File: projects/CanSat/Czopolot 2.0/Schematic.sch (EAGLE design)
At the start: 117 parts

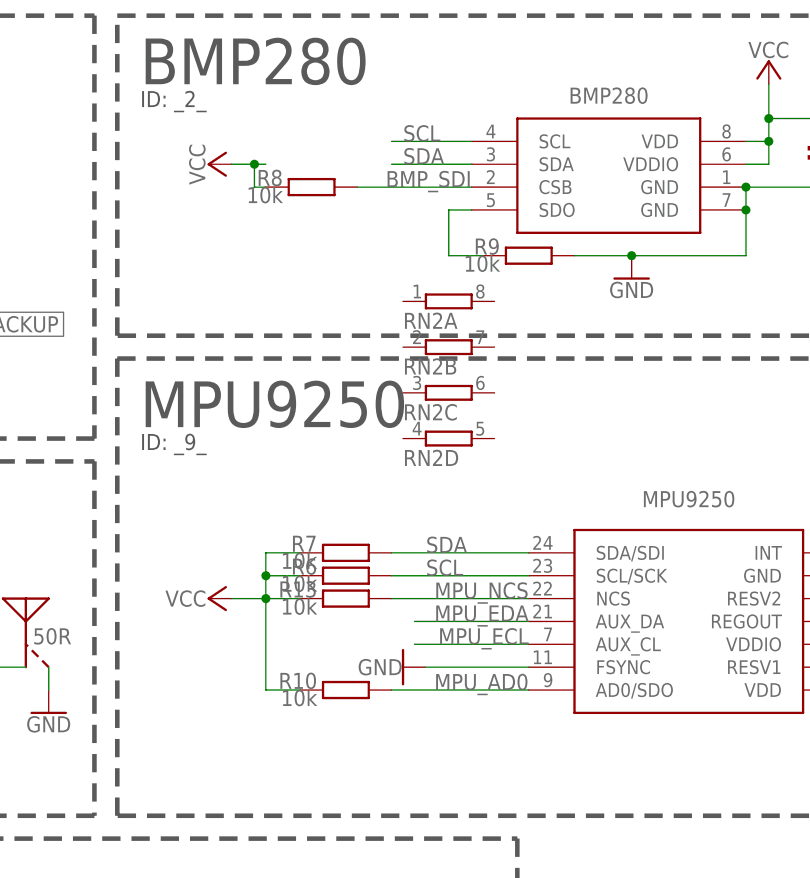
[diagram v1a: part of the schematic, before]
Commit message: Screwholes added
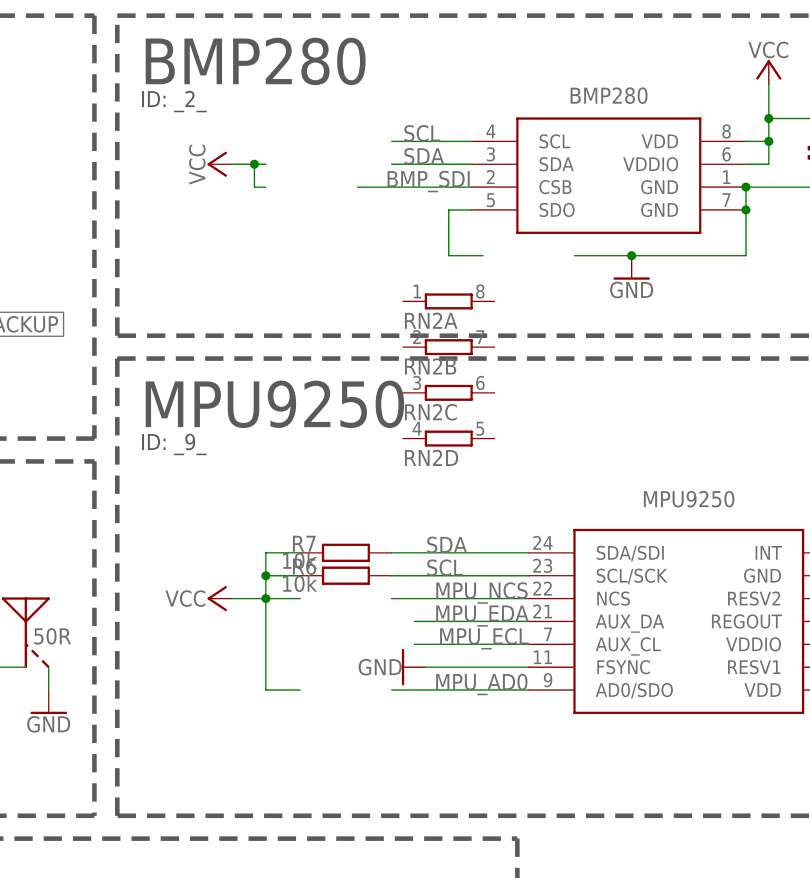
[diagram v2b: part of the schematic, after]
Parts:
- removed R10, R13, R8, R9: 10k, Unified:RESISTOR0603
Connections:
- net BMP_SDI: no longer R8.1
- net BMP_SDO: no longer R9.2
- net GND: no longer R9.1
- net MPU_AD0: no longer R10.1
- net MPU_NCS: no longer R13.1
- net VCC: no longer R10.2, R13.2, R8.2
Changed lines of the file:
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@@
 <part name="GND31" library="supply1" library_urn="urn:adsk.eagle:library:371" deviceset="GND" device=""/>
 <part name="GND32" library="supply1" library_urn="urn:adsk.eagle:library:371" deviceset="GND" device=""/>
-<part name="R8" library="Unified" deviceset="RESISTOR" device="0603" package3d_urn="urn:adsk.eagle:package:23555/3" value="10k"/>
-<part name="R9" library="Unified" deviceset="RESISTOR" device="0603" package3d_urn="urn:adsk.eagle:package:23555/3" value="10k"/>
-<part name="R10" library="Unified" deviceset="RESISTOR" device="0603" package3d_urn="urn:adsk.eagle:package:23555/3" value="10k"/>
-<part name="R13" library="Unified" deviceset="RESISTOR" device="0603" package3d_urn="urn:adsk.eagle:package:23555/3" value="10k"/>
 <part name="U$5" library="SobieskiSat2" deviceset="OSCILLATOR_2PIN" device="32X15" package3d_urn="urn:adsk.eagle:package:16206908/2" value="32.768kHz"/>
 <part name="U$6" library="SobieskiSat2" deviceset="OSCILLATOR_4PIN" device="32X25" package3d_urn="urn:adsk.eagle:package:15725817/1" value="12MHz"/>
@@
 <attribute name="VALUE" x="233.68" y="26.67" size="1.778" layer="96" align="center"/>
 </instance>
-<instance part="R8" gate="R$1" x="226.06" y="80.01" smashed="yes" rot="R90">
-<attribute name="NAME" x="222.885" y="81.915" size="1.778" layer="95" rot="R180"/>
-<attribute name="VALUE" x="222.885" y="80.01" size="1.778" layer="96" rot="R180"/>
-</instance>
-<instance part="R9" gate="R$1" x="250.19" y="72.39" smashed="yes" rot="R90">
-<attribute name="NAME" x="247.015" y="74.295" size="1.778" layer="95" rot="R180"/>
-<attribute name="VALUE" x="247.015" y="72.39" size="1.778" layer="96" rot="R180"/>
-</instance>
-<instance part="R10" gate="R$1" x="229.87" y="24.13" smashed="yes" rot="R90">
-<attribute name="NAME" x="226.695" y="26.035" size="1.778" layer="95" rot="R180"/>
-<attribute name="VALUE" x="226.695" y="24.13" size="1.778" layer="96" rot="R180"/>
-</instance>
-<instance part="R13" gate="R$1" x="229.87" y="34.29" smashed="yes" rot="R90">
-<attribute name="NAME" x="226.695" y="36.195" size="1.778" layer="95" rot="R180"/>
-<attribute name="VALUE" x="226.695" y="34.29" size="1.778" layer="96" rot="R180"/>
-</instance>
 <instance part="U$5" gate="G$1" x="68.58" y="50.8" smashed="yes">
 <attribute name="VALUE" x="68.58" y="55.88" size="1.27" layer="96" align="center"/>
@@
 <pinref part="P+13" gate="VCC" pin="VCC"/>
 <wire x1="217.17" y1="34.29" x2="220.98" y2="34.29" width="0.1524" layer="91"/>
-<pinref part="R10" gate="R$1" pin="2"/>
 <wire x1="220.98" y1="24.13" x2="224.79" y2="24.13" width="0.1524" layer="91"/>
 <wire x1="224.79" y1="34.29" x2="220.98" y2="34.29" width="0.1524" layer="91"/>
-<pinref part="R13" gate="R$1" pin="2"/>
 <pinref part="R7" gate="R$1" pin="2"/>
 <wire x1="224.79" y1="39.37" x2="220.98" y2="39.37" width="0.1524" layer="91"/>
@@
 <wire x1="220.98" y1="82.55" x2="219.71" y2="82.55" width="0.1524" layer="91"/>
 <junction x="219.71" y="82.55"/>
-<pinref part="R8" gate="R$1" pin="2"/>
 <wire x1="219.71" y1="82.55" x2="219.71" y2="80.01" width="0.1524" layer="91"/>
 <wire x1="219.71" y1="80.01" x2="220.98" y2="80.01" width="0.1524" layer="91"/>
@@
 </segment>
 <segment>
-<pinref part="R9" gate="R$1" pin="1"/>
 <pinref part="U$8" gate="G$1" pin="GND@2"/>
 <wire x1="255.27" y1="72.39" x2="261.62" y2="72.39" width="0.1524" layer="91"/>
@@
 <wire x1="243.84" y1="80.01" x2="231.14" y2="80.01" width="0.1524" layer="91"/>
 <label x="243.84" y="80.01" size="1.778" layer="95" align="bottom-right"/>
-<pinref part="R8" gate="R$1" pin="1"/>
 </segment>
 </net>
@@
 <wire x1="241.3" y1="77.47" x2="241.3" y2="72.39" width="0.1524" layer="91"/>
 <wire x1="241.3" y1="72.39" x2="245.11" y2="72.39" width="0.1524" layer="91"/>
-<pinref part="R9" gate="R$1" pin="2"/>
 </segment>
 </net>
@@
 <wire x1="250.19" y1="34.29" x2="234.95" y2="34.29" width="0.1524" layer="91"/>
 <label x="250.19" y="34.29" size="1.778" layer="95" align="bottom-right"/>
-<pinref part="R13" gate="R$1" pin="1"/>
 </segment>
 </net>
@@
 <wire x1="234.95" y1="24.13" x2="250.19" y2="24.13" width="0.1524" layer="91"/>
 <label x="250.19" y="24.13" size="1.778" layer="95" align="bottom-right"/>
-<pinref part="R10" gate="R$1" pin="1"/>
-</segment>
-</net>
+</segment>
+</net>

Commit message: Version 0.5
Pre-final component placement
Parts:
- removed C38, C39: big_pol, Unified:CAPACITOR0603
- removed C5: 4.7u, Unified:CAPACITOR0603
- added U$33, U$34: PADOCT, Unified:PADOCT
- BAT_PACK: device SobieskiSat2:BATTERYDIP -> SobieskiSat2:BATTERYBIG
- BTN_DFU: value PUSH-SWITCH -> PUSH-SWITCHDIP; device SobieskiSat2:PUSH-SWITCH -> SobieskiSat2:PUSH-SWITCHDIP
- U$19, U$29, U$31, U$32: value PAD -> PADRND; device Unified:PAD -> Unified:PADRND
- U$20, U$30: value PAD -> PADOCT; device Unified:PAD -> Unified:PADOCT
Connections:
- net GND: now also U$33.1, U$34.1; no longer C38.1, C39.1, C5.2, U$32.1
- net VCC: now also U$32.1; no longer C5.1
- net VSYS: no longer C38.2, C39.2
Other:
- note added: "4.7u was there"

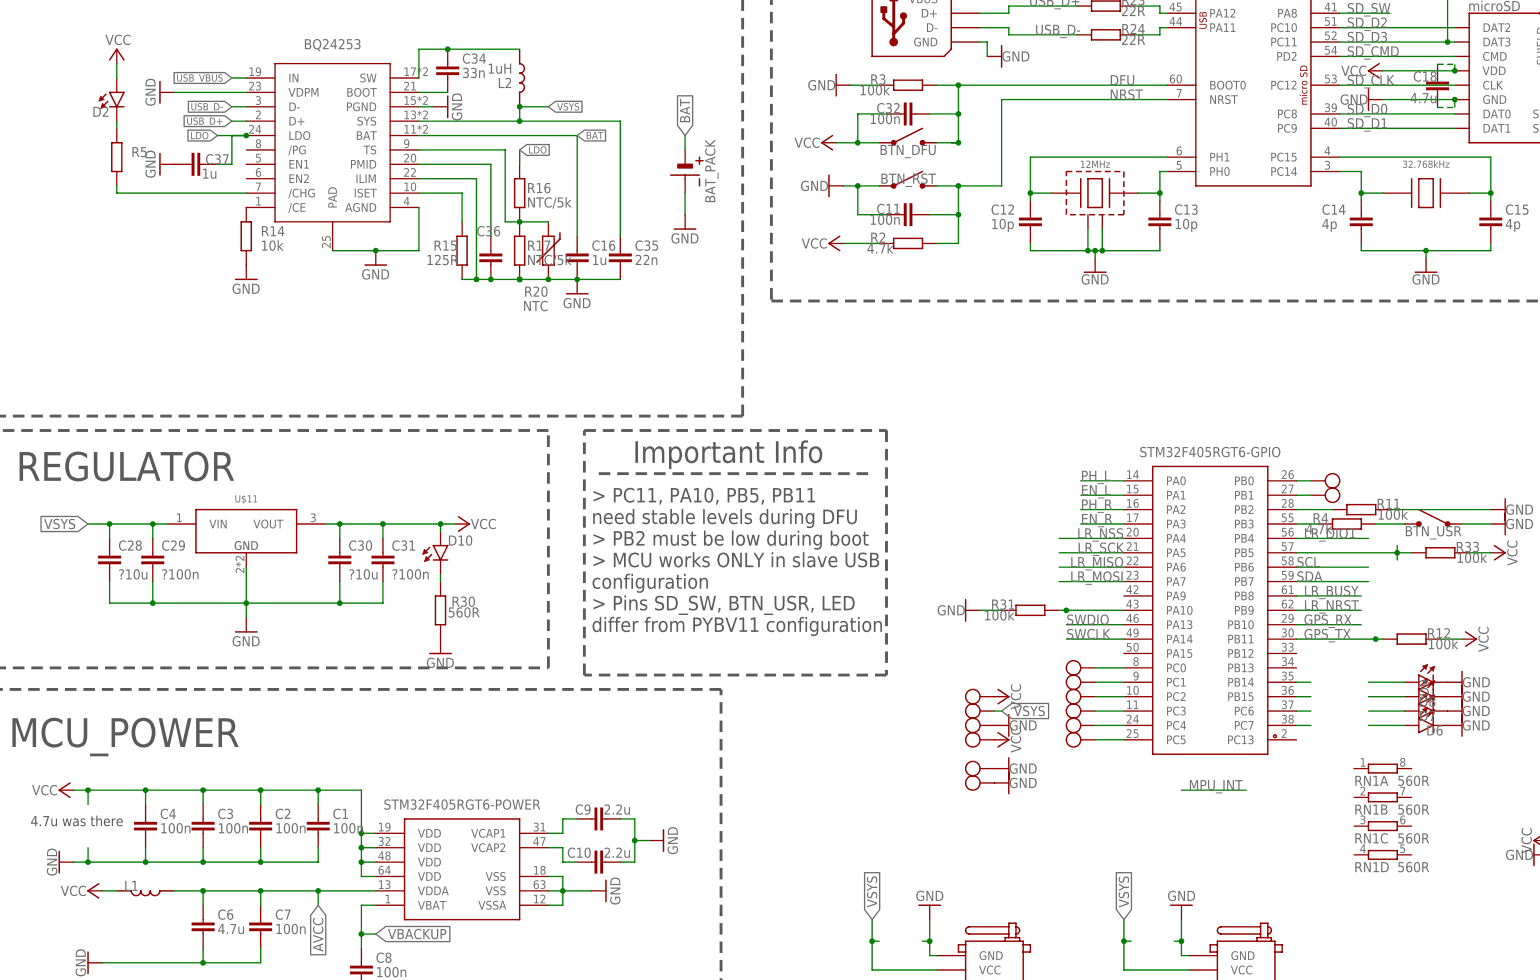
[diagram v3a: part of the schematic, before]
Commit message: Round traces test
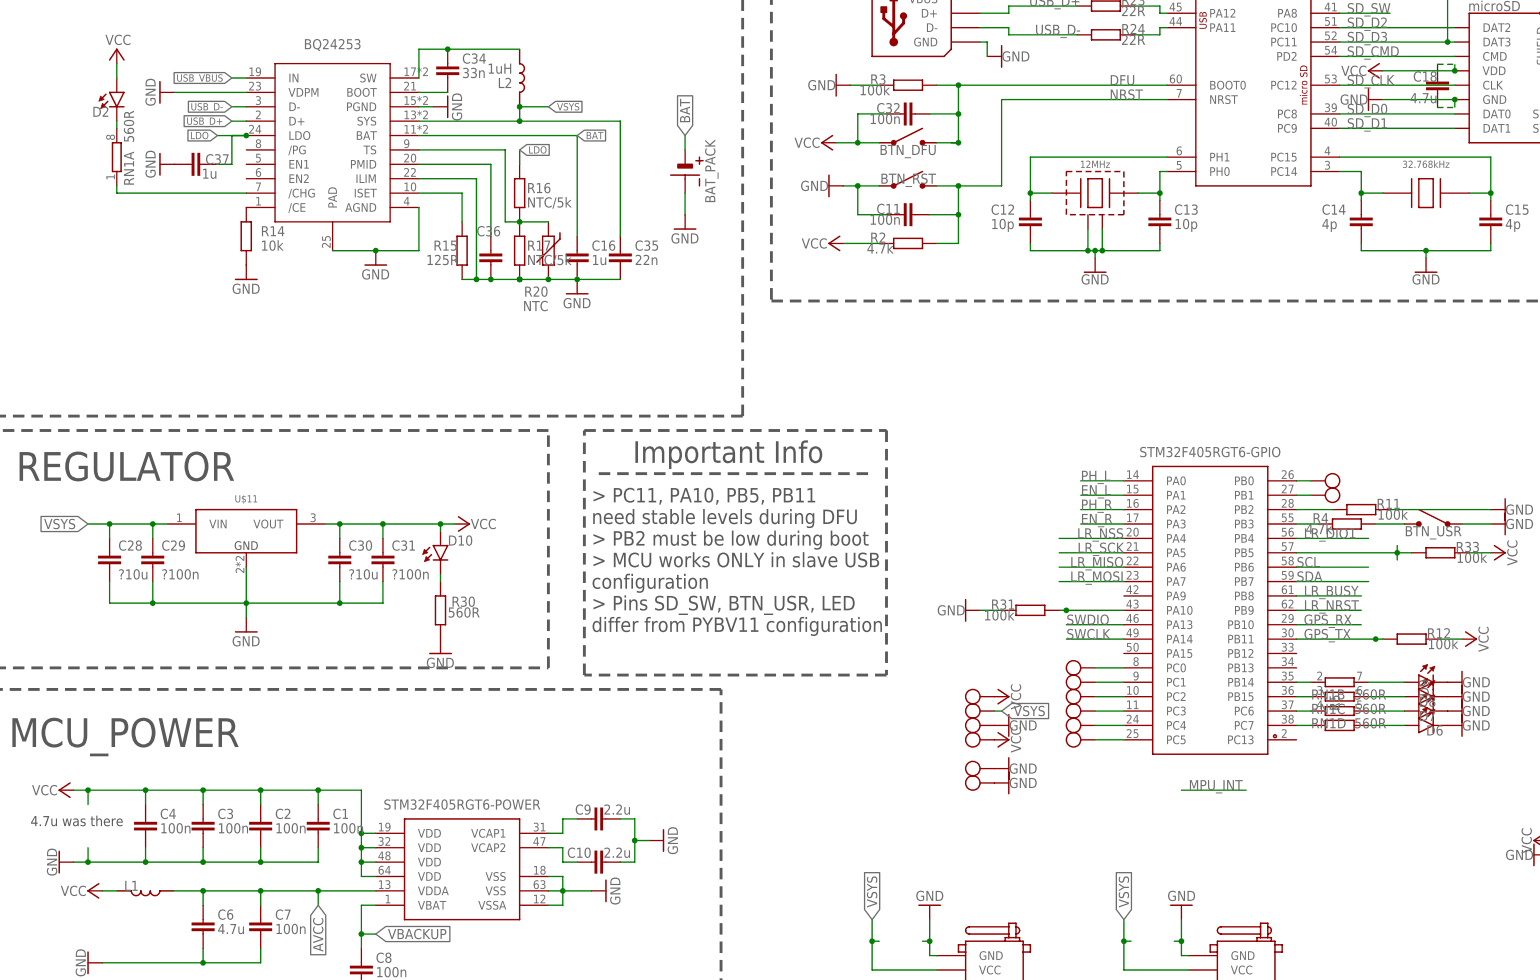
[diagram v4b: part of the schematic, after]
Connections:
- net N$1: now also RN1B.2
- net N$10: now also RN1A.1; no longer R5.1
- net N$15: now also R5.2
- net N$19: now also RN1D.1
- net N$2: now also RN1C.2
- net N$20: now also RN1C.1
- net N$28: now also RN1B.1
- net N$3: now also RN1A.2; no longer R5.2
- net N$37: now also RN1D.2
- net N$38: now also R5.1
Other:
- moved on the sheet: R5, RN1A, RN1B, RN1C, RN1D
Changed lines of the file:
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@@
 <setting verticaltext="up"/>
 </settings>
-<grid distance="0.1" unitdist="inch" unit="inch" style="lines" multiple="1" display="no" altdistance="0.01" altunitdist="inch" altunit="inch"/>
+<grid distance="0.05" unitdist="inch" unit="inch" style="lines" multiple="1" display="no" altdistance="0.01" altunitdist="inch" altunit="inch"/>
 <layers>
 <layer number="1" name="Top" color="4" fill="1" visible="no" active="no"/>
@@
 <part name="GND19" library="supply1" library_urn="urn:adsk.eagle:library:371" deviceset="GND" device=""/>
 <part name="U$10" library="SobieskiSat2" deviceset="BQ24253" device="" package3d_urn="urn:adsk.eagle:package:15841520/1"/>
-<part name="R5" library="Unified" deviceset="RESISTOR" device="0603" package3d_urn="urn:adsk.eagle:package:23555/3"/>
 <part name="R14" library="Unified" deviceset="RESISTOR" device="0603" package3d_urn="urn:adsk.eagle:package:23555/3" value="10k"/>
 <part name="R15" library="Unified" deviceset="RESISTOR" device="0603" package3d_urn="urn:adsk.eagle:package:23555/3" value="125R"/>
@@
 <part name="U$34" library="Unified" deviceset="PAD" device="OCT" value="PADOCT"/>
 <part name="GND45" library="supply1" library_urn="urn:adsk.eagle:library:371" deviceset="GND" device=""/>
+<part name="R5" library="Unified" deviceset="RESISTOR" device="0603" package3d_urn="urn:adsk.eagle:package:23555/3"/>
 </parts>
 <sheets>
@@
 </instance>
 <instance part="U$10" gate="G$1" x="-124.46" y="58.42" smashed="yes"/>
-<instance part="R5" gate="R$1" x="-162.56" y="57.15" smashed="yes">
-<attribute name="NAME" x="-160.02" y="57.15" size="1.778" layer="95"/>
-<attribute name="VALUE" x="-160.02" y="54.61" size="1.778" layer="96"/>
-</instance>
 <instance part="R14" gate="R$1" x="-139.7" y="43.18" smashed="yes">
 <attribute name="NAME" x="-137.16" y="43.18" size="1.778" layer="95"/>
@@
 <attribute name="VALUE" x="-86.36" y="31.75" size="1.778" layer="96" rot="R180"/>
 </instance>
-<instance part="RN1" gate="A" x="60.96" y="-50.8" smashed="yes">
-<attribute name="VALUE" x="63.5" y="-53.848" size="1.778" layer="96"/>
-<attribute name="NAME" x="55.88" y="-53.848" size="1.778" layer="95"/>
-</instance>
-<instance part="RN1" gate="B" x="60.96" y="-55.88" smashed="yes">
-<attribute name="VALUE" x="63.5" y="-58.928" size="1.778" layer="96"/>
-<attribute name="NAME" x="55.88" y="-58.928" size="1.778" layer="95"/>
-</instance>
-<instance part="RN1" gate="C" x="60.96" y="-60.96" smashed="yes">
-<attribute name="VALUE" x="63.5" y="-64.008" size="1.778" layer="96"/>
-<attribute name="NAME" x="55.88" y="-64.008" size="1.778" layer="95"/>
-</instance>
-<instance part="RN1" gate="D" x="60.96" y="-66.04" smashed="yes">
-<attribute name="VALUE" x="63.5" y="-69.088" size="1.778" layer="96"/>
-<attribute name="NAME" x="55.88" y="-69.088" size="1.778" layer="95"/>
+<instance part="RN1" gate="A" x="-162.56" y="57.15" smashed="yes" rot="R90">
+<attribute name="VALUE" x="-159.512" y="59.69" size="1.778" layer="96" rot="R90"/>
+<attribute name="NAME" x="-159.512" y="52.07" size="1.778" layer="95" rot="R90"/>
+</instance>
+<instance part="RN1" gate="B" x="53.34" y="-35.56" smashed="yes">
+<attribute name="VALUE" x="55.88" y="-38.608" size="1.778" layer="96"/>
+<attribute name="NAME" x="48.26" y="-38.608" size="1.778" layer="95"/>
+</instance>
+<instance part="RN1" gate="C" x="53.34" y="-38.1" smashed="yes">
+<attribute name="VALUE" x="55.88" y="-41.148" size="1.778" layer="96"/>
+<attribute name="NAME" x="48.26" y="-41.148" size="1.778" layer="95"/>
+</instance>
+<instance part="RN1" gate="D" x="53.34" y="-40.64" smashed="yes">
+<attribute name="VALUE" x="55.88" y="-43.688" size="1.778" layer="96"/>
+<attribute name="NAME" x="48.26" y="-43.688" size="1.778" layer="95"/>
 </instance>
 <instance part="RN2" gate="A" x="241.3" y="67.31" smashed="yes">
@@
 <instance part="GND45" gate="1" x="-5.08" y="-53.34" smashed="yes" rot="MR270">
 <attribute name="VALUE" x="-2.54" y="-53.34" size="1.778" layer="96" rot="MR180" align="center"/>
+</instance>
+<instance part="R5" gate="R$1" x="53.34" y="-43.18" smashed="yes" rot="R90">
+<attribute name="NAME" x="53.34" y="-40.64" size="1.778" layer="95" rot="R90"/>
+<attribute name="VALUE" x="55.88" y="-40.64" size="1.778" layer="96" rot="R90"/>
 </instance>
 </instances>
@@
 <pinref part="D9" gate="G$1" pin="P$1"/>
 <wire x1="58.42" y1="-35.56" x2="64.77" y2="-35.56" width="0.1524" layer="91"/>
+<pinref part="RN1" gate="B" pin="2"/>
 </segment>
 </net>
@@
 <pinref part="D8" gate="G$1" pin="P$1"/>
 <wire x1="58.42" y1="-38.1" x2="64.77" y2="-38.1" width="0.1524" layer="91"/>
+<pinref part="RN1" gate="C" pin="2"/>
 </segment>
 </net>
@@
 <pinref part="D7" gate="G$1" pin="P$1"/>
 <wire x1="58.42" y1="-40.64" x2="64.77" y2="-40.64" width="0.1524" layer="91"/>
+<pinref part="RN1" gate="D" pin="2"/>
 </segment>
 </net>
@@
 <pinref part="D6" gate="G$1" pin="P$1"/>
 <wire x1="58.42" y1="-43.18" x2="64.77" y2="-43.18" width="0.1524" layer="91"/>
+<pinref part="R5" gate="R$1" pin="1"/>
 </segment>
 </net>
@@
 <segment>
 <pinref part="D2" gate="G$1" pin="P$2"/>
-<pinref part="R5" gate="R$1" pin="2"/>
 <wire x1="-162.56" y1="63.5" x2="-162.56" y2="62.23" width="0.1524" layer="91"/>
+<pinref part="RN1" gate="A" pin="2"/>
 </segment>
 </net>
 <net name="N$10" class="0">
 <segment>
-<pinref part="R5" gate="R$1" pin="1"/>
 <wire x1="-162.56" y1="52.07" x2="-162.56" y2="50.8" width="0.1524" layer="91"/>
 <pinref part="U$10" gate="G$1" pin="/CHG"/>
 <wire x1="-162.56" y1="50.8" x2="-139.7" y2="50.8" width="0.1524" layer="91"/>
+<pinref part="RN1" gate="A" pin="1"/>
 </segment>
 </net>
@@
 <pinref part="U$1" gate="STM32F405RGT6_GPIO" pin="PC7"/>
 <wire x1="48.26" y1="-43.18" x2="45.72" y2="-43.18" width="0.1524" layer="91"/>
+<pinref part="R5" gate="R$1" pin="2"/>
 </segment>
 </net>
@@
 <pinref part="U$1" gate="STM32F405RGT6_GPIO" pin="PC6"/>
 <wire x1="48.26" y1="-40.64" x2="45.72" y2="-40.64" width="0.1524" layer="91"/>
+<pinref part="RN1" gate="D" pin="1"/>
 </segment>
 </net>
@@
 <pinref part="U$1" gate="STM32F405RGT6_GPIO" pin="PB15"/>
 <wire x1="48.26" y1="-38.1" x2="45.72" y2="-38.1" width="0.1524" layer="91"/>
+<pinref part="RN1" gate="C" pin="1"/>
 </segment>
 </net>
@@
 <pinref part="U$1" gate="STM32F405RGT6_GPIO" pin="PB14"/>
 <wire x1="48.26" y1="-35.56" x2="45.72" y2="-35.56" width="0.1524" layer="91"/>
-</segment>
-</net>
+<pinref part="RN1" gate="B" pin="1"/>
+</segment>
+</net>

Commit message: Pads backup
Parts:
- removed U$16: SERVO, Unified:SERVO
- added R8: 10k, Unified:RESISTOR0603
- RN2: value (none) -> 10k
- U$13: value SERVO -> GPIO_PADS; device Unified:SERVO -> SobieskiSat2:GPIO_PADS
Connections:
- removed net N$41: U$13.SIG
- removed net N$42: U$16.SIG
- removed net N$49: U$1STM32F405RGT6_GPIO.PC4, U$27.1
- new net DAC: U$1STM32F405RGT6_GPIO.PA4, U$27.1
- net BMP_SDI: now also RN2A.1
- net BMP_SDO: now also RN2B.2
- net GND: now also RN2B.1; no longer U$13.GND, U$16.GND
- net LR_NSS: now also U$1STM32F405RGT6_GPIO.PC4; no longer U$1STM32F405RGT6_GPIO.PA4
- net MPU_AD0: now also R8.1
- net MPU_NCS: now also RN2C.1
- net N$28: now also U$1STM32F405RGT6_GPIO.PB12; no longer U$1STM32F405RGT6_GPIO.PB14
- net VCC: now also R8.2, RN2A.2, RN2C.2
- net VSYS: no longer U$13.VCC, U$16.VCC
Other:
- moved on the sheet: D9, RN1B, RN2A, RN2B, RN2C, RN2D
